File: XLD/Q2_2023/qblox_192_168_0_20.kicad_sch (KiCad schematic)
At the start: 11 parts

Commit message: mend
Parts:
- renumbered IP602 to IP2, QCM601 to QCM4, QRM_RF601 to QCM5, QRM_RF601 to QCM6, QCM_RF604 to QCM_RF4, QCM602 to QRM1, QRM_RF601 to QRM_RF3, QRM_RF601 to QRM_RF4, SC601 to SC3, SC602 to SC4
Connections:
- net at QCM6. (o4): now also IP2. (9)
- net at IP2. (9): now also QRM_RF3. (o1); no longer QCM6. (o4)
- net at QCM_RF4. (o2): now also SC3.; no longer SC4.
- net at QCM5. (o4): now also IP2. (9)
- net at QRM1. (o4): now also IP2. (9)
- new net: QRM_RF4. (o1), SC4.
- new net: QCM_RF4. (o2), SC4.
- new net: IP2. (9), QRM_RF4. (o1)
- new net: IP2. (9), QCM_RF4. (o2)
- new net: IP2. (9), QCM4. (Trig)
- new net: QRM_RF3. (o1), SC3.
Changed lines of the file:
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@@
   (symbol (lib_id "Quantum Computing:QBlox_QCM") (at 477.52 137.795 0) (unit 1)
     (in_bom yes) (on_board no) (dnp no) (fields_autoplaced)
-    (property "Reference" "QRM_RF601" (at 475.615 139.827 0)
+    (property "Reference" "QCM6" (at 475.615 139.827 0)
       (effects (font (size 1.27 1.27)) (justify left))
     )
@@
   (symbol (lib_id "Quantum Computing:Splitter_Combiner") (at 452.755 166.37 180) (unit 1)
     (in_bom yes) (on_board no) (dnp no) (fields_autoplaced)
-    (property "Reference" "SC602" (at 452.755 158.75 0)
+    (property "Reference" "SC4" (at 452.755 158.75 0)
       (effects (font (size 1.27 1.27)))
     )
@@
   (symbol (lib_id "Quantum Computing:QBlox_QRM_RF") (at 457.835 137.795 0) (unit 1)
     (in_bom yes) (on_board no) (dnp no) (fields_autoplaced)
-    (property "Reference" "QRM_RF601" (at 455.93 139.827 0)
+    (property "Reference" "QRM_RF4" (at 455.93 139.827 0)
       (effects (font (size 1.27 1.27)) (justify left))
     )
@@
   (symbol (lib_id "Quantum Computing:QBlox_QCM") (at 379.095 137.795 0) (unit 1)
     (in_bom yes) (on_board no) (dnp no) (fields_autoplaced)
-    (property "Reference" "QRM_RF601" (at 377.19 139.827 0)
+    (property "Reference" "QCM5" (at 377.19 139.827 0)
       (effects (font (size 1.27 1.27)) (justify left))
     )
@@
   (symbol (lib_id "Quantum Computing:QBlox_QRM") (at 142.875 137.795 0) (unit 1)
     (in_bom yes) (on_board no) (dnp no) (fields_autoplaced)
-    (property "Reference" "QCM602" (at 140.97 139.827 0)
+    (property "Reference" "QRM1" (at 140.97 139.827 0)
       (effects (font (size 1.27 1.27)) (justify left))
     )
@@
   (symbol (lib_id "Quantum Computing:QBlox_QCM_RF") (at 339.725 137.795 0) (unit 1)
     (in_bom yes) (on_board no) (dnp no) (fields_autoplaced)
-    (property "Reference" "QCM_RF604" (at 337.82 139.827 0)
+    (property "Reference" "QCM_RF4" (at 337.82 139.827 0)
       (effects (font (size 1.27 1.27)) (justify left))
     )
@@
   (symbol (lib_id "Quantum Computing:Qblox_Cluster") (at 300.355 116.84 0) (unit 1)
     (in_bom yes) (on_board yes) (dnp no) (fields_autoplaced)
-    (property "Reference" "IP602" (at 300.355 109.855 0)
+    (property "Reference" "IP2" (at 300.355 109.855 0)
       (effects (font (size 1.27 1.27)))
     )
@@
   (symbol (lib_id "Quantum Computing:QBlox_CTRL") (at 102.235 137.795 0) (unit 1)
     (in_bom yes) (on_board no) (dnp no) (fields_autoplaced)
-    (property "Reference" "QCM601" (at 100.33 139.827 0)
+    (property "Reference" "QCM4" (at 100.33 139.827 0)
       (effects (font (size 1.27 1.27)) (justify left))
     )
@@
   (symbol (lib_id "Quantum Computing:QBlox_QRM_RF") (at 418.465 137.795 0) (unit 1)
     (in_bom yes) (on_board no) (dnp no) (fields_autoplaced)
-    (property "Reference" "QRM_RF601" (at 416.56 139.827 0)
+    (property "Reference" "QRM_RF3" (at 416.56 139.827 0)
       (effects (font (size 1.27 1.27)) (justify left))
     )
@@
   (symbol (lib_id "Quantum Computing:Splitter_Combiner") (at 422.275 166.37 180) (unit 1)
     (in_bom yes) (on_board no) (dnp no) (fields_autoplaced)
-    (property "Reference" "SC601" (at 422.275 158.75 0)
-      (effects (font (size 1.27 1.27)))
-    )
+    (property "Reference" "SC3" (at 422.275 158.75 0)
+      (effects (font (size 1.27 1.27)))
+    )

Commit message: more updates
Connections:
- net at QCM6. (o4): now also IP2. (9)
- net at IP2. (9): now also QRM_RF3. (o1); no longer QCM6. (o4)
- net at QCM_RF4. (o2): now also SC3.; no longer SC4.
- net at QCM5. (o4): now also IP2. (9)
- net at QRM1. (o4): now also IP2. (9)
- new net: QRM_RF4. (o1), SC4.
- new net: QCM_RF4. (o2), SC4.
- new net: IP2. (9), QRM_RF4. (o1)
- new net: IP2. (9), QCM_RF4. (o2)
- new net: IP2. (9), QCM4. (Trig)
- new net: QRM_RF3. (o1), SC3.

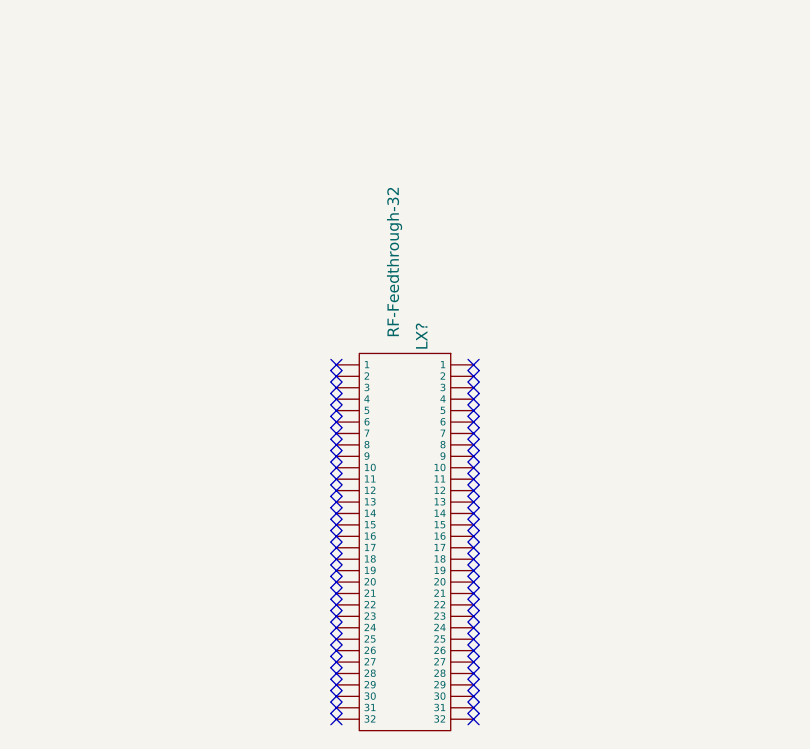
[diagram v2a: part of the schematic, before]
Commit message: update attenuators and pumplines
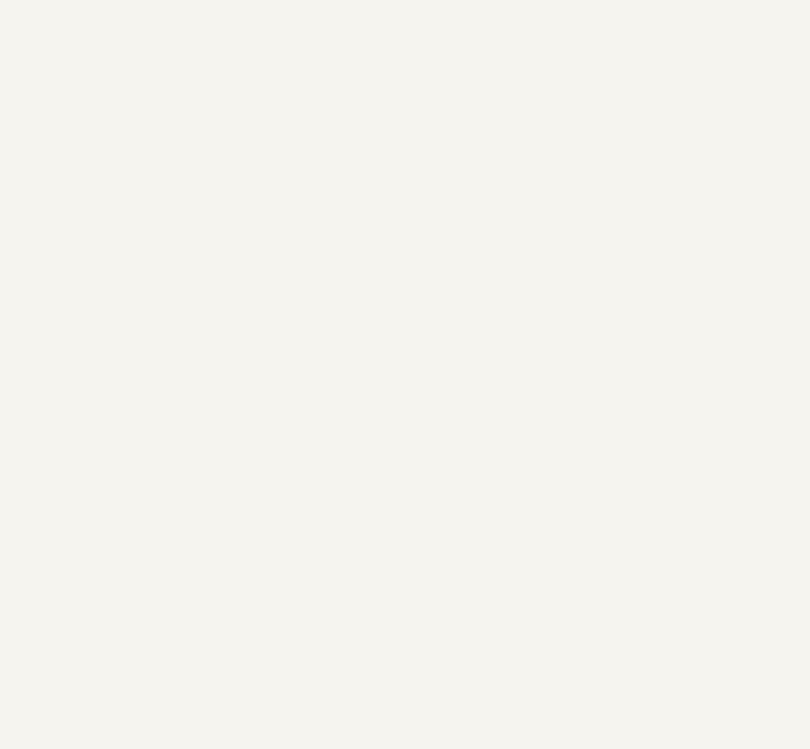
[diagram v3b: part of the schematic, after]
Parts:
- removed LX?: RF-Feedthrough-32, symbol Quantum Computing:RF-Feedthrough-32
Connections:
- net at QCM6. (o4): now also IP2. (9)
- net at IP2. (9): now also QRM_RF3. (o1); no longer QCM6. (o4)
- net at QCM_RF4. (o2): now also SC3.; no longer SC4.
- net at QCM5. (o4): now also IP2. (9)
- net at QRM1. (o4): now also IP2. (9)
- new net: QRM_RF4. (o1), SC4.
- new net: QCM_RF4. (o2), SC4.
- new net: IP2. (9), QRM_RF4. (o1)
- new net: IP2. (9), QCM_RF4. (o2)
- new net: IP2. (9), QCM4. (Trig)
- new net: QRM_RF3. (o1), SC3.
- no-connect marks 79 -> 15
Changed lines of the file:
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@@
 (kicad_sch (version 20230121) (generator eeschema)
   (paper "A2")
-  (no_connect (at 322.58 280.67))
   (no_connect (at 139.065 132.08))
-  (no_connect (at 322.58 292.1))
   (no_connect (at 139.065 133.35))
-  (no_connect (at 307.34 266.7))
-  (no_connect (at 322.58 287.02))
-  (no_connect (at 307.34 276.86))
   (no_connect (at 98.425 134.62))
-  (no_connect (at 307.34 278.13))
-  (no_connect (at 307.34 273.05))
-  (no_connect (at 322.58 269.24))
-  (no_connect (at 322.58 274.32))
-  (no_connect (at 307.34 293.37))
-  (no_connect (at 307.34 297.18))
   (no_connect (at 139.065 134.62))
-  (no_connect (at 307.34 300.99))
-  (no_connect (at 307.34 270.51))
-  (no_connect (at 322.58 290.83))
-  (no_connect (at 322.58 270.51))
-  (no_connect (at 307.34 275.59))
-  (no_connect (at 322.58 298.45))
-  (no_connect (at 307.34 302.26))
   (no_connect (at 375.285 134.62))
-  (no_connect (at 307.34 281.94))
   (no_connect (at 375.285 133.35))
-  (no_connect (at 322.58 303.53))
-  (no_connect (at 322.58 267.97))
-  (no_connect (at 307.34 284.48))
-  (no_connect (at 322.58 302.26))
-  (no_connect (at 307.34 292.1))
-  (no_connect (at 307.34 294.64))
   (no_connect (at 98.425 133.35))
-  (no_connect (at 307.34 265.43))
-  (no_connect (at 307.34 303.53))
   (no_connect (at 473.71 133.35))
   (no_connect (at 375.285 135.89))
-  (no_connect (at 322.58 279.4))
-  (no_connect (at 307.34 269.24))
   (no_connect (at 375.285 132.08))
-  (no_connect (at 307.34 289.56))
   (no_connect (at 473.71 134.62))
   (no_connect (at 98.425 135.89))
-  (no_connect (at 322.58 300.99))
-  (no_connect (at 322.58 299.72))
   (no_connect (at 473.71 135.89))
-  (no_connect (at 307.34 304.8))
-  (no_connect (at 307.34 280.67))
   (no_connect (at 139.065 135.89))
-  (no_connect (at 322.58 275.59))
-  (no_connect (at 322.58 271.78))
-  (no_connect (at 307.34 285.75))
-  (no_connect (at 322.58 297.18))
-  (no_connect (at 322.58 295.91))
-  (no_connect (at 307.34 267.97))
-  (no_connect (at 322.58 266.7))
-  (no_connect (at 322.58 283.21))
-  (no_connect (at 322.58 288.29))
-  (no_connect (at 322.58 265.43))
-  (no_connect (at 307.34 274.32))
-  (no_connect (at 307.34 283.21))
-  (no_connect (at 307.34 288.29))
-  (no_connect (at 307.34 279.4))
-  (no_connect (at 307.34 298.45))
-  (no_connect (at 322.58 284.48))
-  (no_connect (at 322.58 289.56))
-  (no_connect (at 322.58 273.05))
-  (no_connect (at 307.34 287.02))
-  (no_connect (at 322.58 276.86))
-  (no_connect (at 307.34 290.83))
-  (no_connect (at 322.58 294.64))
-  (no_connect (at 307.34 299.72))
-  (no_connect (at 322.58 281.94))
-  (no_connect (at 307.34 295.91))
-  (no_connect (at 307.34 271.78))
-  (no_connect (at 322.58 293.37))
-  (no_connect (at 322.58 285.75))
-  (no_connect (at 322.58 278.13))
-  (no_connect (at 322.58 304.8))
   (no_connect (at 473.71 132.08))
   (wire (pts (xy 467.36 166.37) (xy 467.36 146.05))
@@
         )
       )
-    )
-  )
-  (symbol (lib_id "Quantum Computing:RF-Feedthrough-32") (at 314.96 285.115 270) (unit 1)
-    (in_bom yes) (on_board yes) (dnp no) (fields_autoplaced)
-    (property "Reference" "LX?" (at 316.865 262.255 0)
-      (effects (font (size 1.27 1.27)))
-    )
-    (property "Value" "RF-Feedthrough-32" (at 313.69 254 0)
-      (effects (font (size 1.27 1.27)))
-    )
-    (property "Footprint" "" (at 314.96 285.115 0)
-      (effects (font (size 1.27 1.27)) hide)
-    )
-    (property "Datasheet" "" (at 314.96 285.115 0)
-      (effects (font (size 1.27 1.27)) hide)
-    )
-    (pin "")
-    (pin "")
-    (pin "")
-    (pin "")
-    (pin "")
-    (pin "")
-    (pin "")
-    (pin "")
-    (pin "")
-    (pin "")
-    (pin "")
-    (pin "")
-    (pin "")
-    (pin "")
-    (pin "")
-    (pin "")
-    (pin "")
-    (pin "")
-    (pin "")
-    (pin "")
-    (pin "")
-    (pin "")
-    (pin "")
-    (pin "")
-    (pin "")
-    (pin "")
-    (pin "")
-    (pin "")
-    (pin "")
-    (pin "")
-    (pin "")
-    (pin "")
-    (pin "")
-    (pin "")
-    (pin "")
-    (pin "")
-    (pin "")
-    (pin "")
-    (pin "")
-    (pin "")
-    (pin "")
-    (pin "")
-    (pin "")
-    (pin "")
-    (pin "")
-    (pin "")
-    (pin "")
-    (pin "")
-    (pin "")
-    (pin "")
-    (pin "")
-    (pin "")
-    (pin "")
-    (pin "")
-    (pin "")
-    (pin "")
-    (pin "")
-    (pin "")
-    (pin "")
-    (pin "")
-    (pin "")
-    (pin "")
-    (pin "")
-    (pin "")
-    (instances
-      (project "Q2_2023"
-        (path "/9924af8b-9fcb-4325-a1dc-18dd2c4184d7/07777306-87c2-4eb9-aeba-eeffc6ad9af4"
-          (reference "LX?") (unit 1)
-        )
-        (path "/9924af8b-9fcb-4325-a1dc-18dd2c4184d7/cbbd5daf-170b-465d-a354-f5302933c82d/5f7bbf44-23f7-4598-b2ea-f90c8a43578e"
-          (reference "LX2") (unit 1)
-        )
-      )

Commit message: Improvements to library components, title, date
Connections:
- net at QCM6. (o4): now also IP2. (9)
- net at IP2. (9): now also QRM_RF3. (o1); no longer QCM6. (o4)
- net at QCM_RF4. (o2): now also SC3.; no longer SC4.
- net at QCM5. (o4): now also IP2. (9)
- net at QRM1. (o4): now also IP2. (9)
- new net: QRM_RF4. (o1), SC4.
- new net: QCM_RF4. (o2), SC4.
- new net: IP2. (9), QRM_RF4. (o1)
- new net: IP2. (9), QCM_RF4. (o2)
- new net: IP2. (9), QCM4. (Trig)
- new net: QRM_RF3. (o1), SC3.
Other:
- company: (none) -> Technology Innovation Institute
- title: (none) -> XLD Setup Q2 2023
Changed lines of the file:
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@@
 (kicad_sch (version 20230121) (generator eeschema)
   (paper "A2")
+  (title_block
+    (title "XLD Setup Q2 2023")
+    (date "2023-06-14")
+    (company "Technology Innovation Institute")
+  )
   (no_connect (at 139.065 132.08))
   (no_connect (at 139.065 133.35))

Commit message: Correction in line numbers of QW 25Q
We have checked the cables of QW 25Q by connecting the IN and OUT lines to VNA and found that there is are corrections required in the line numbers mentioned in the drawing. Below are the correction made:

QW P14 - In line L3-30 , Out line L2-1
QW P29 - In line L3-26 , Out line L2-2
QW P44 - In line L3-27 , Out line L2-3
QW P59 - In line L3-18 , Out line L2-4

The Coupler pump line L3-21 replaced with L3-29
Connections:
- net at QCM6. (o4): now also IP2. (9)
- net at IP2. (9): now also QRM_RF3. (o1); no longer QCM6. (o4)
- net at QCM_RF4. (o2): now also SC3.; no longer SC4.
- net at QCM5. (o4): now also IP2. (9)
- net at QRM1. (o4): now also IP2. (9)
- new net: QRM_RF4. (o1), SC4.
- new net: QCM_RF4. (o2), SC4.
- new net: IP2. (9), QRM_RF4. (o1)
- new net: IP2. (9), QCM_RF4. (o2)
- new net: IP2. (9), QCM4. (Trig)
- new net: QRM_RF3. (o1), SC3.

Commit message: fix qw5q twpa pump line ip address
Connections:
- net at QCM6. (o4): now also IP2. (9)
- net at IP2. (9): now also QRM_RF3. (o1); no longer QCM6. (o4)
- net at QCM_RF4. (o2): now also SC3.; no longer SC4.
- net at QCM5. (o4): now also IP2. (9)
- net at QRM1. (o4): now also IP2. (9)
- new net: QRM_RF4. (o1), SC4.
- new net: QCM_RF4. (o2), SC4.
- new net: IP2. (9), QRM_RF4. (o1)
- new net: IP2. (9), QCM_RF4. (o2)
- new net: IP2. (9), QCM4. (Trig)
- new net: QRM_RF3. (o1), SC3.

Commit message: ip for LO18
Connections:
- net at QCM6. (o4): now also IP2. (9)
- net at IP2. (9): now also QRM_RF3. (o1); no longer QCM6. (o4)
- net at QCM_RF4. (o2): now also SC3.; no longer SC4.
- net at QCM5. (o4): now also IP2. (9)
- net at QRM1. (o4): now also IP2. (9)
- new net: QRM_RF4. (o1), SC4.
- new net: QCM_RF4. (o2), SC4.
- new net: IP2. (9), QRM_RF4. (o1)
- new net: IP2. (9), QCM_RF4. (o2)
- new net: IP2. (9), QCM4. (Trig)
- new net: QRM_RF3. (o1), SC3.
